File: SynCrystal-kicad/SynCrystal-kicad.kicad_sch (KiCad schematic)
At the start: 8 parts, among them Q1 BC847, U2 74HC14

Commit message: the opamp
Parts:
- added C2, C4: 100n, Capacitor_SMD:C_0805_2012Metric, symbol Device:C_Small
- added C3: 1u, Capacitor_SMD:C_0805_2012Metric, symbol Device:C_Small
- added R10: 2k2, Resistor_SMD:R_0805_2012Metric, symbol Device:R_Small
- added R11: 100, Resistor_SMD:R_0805_2012Metric, symbol Device:R_Small
- added R12: 12, Resistor_SMD:R_0805_2012Metric, symbol Device:R_Small
- added R13: 4k7, Resistor_SMD:R_0805_2012Metric, symbol Device:R_Small
- added R14, R9: 10k, Resistor_SMD:R_0805_2012Metric, symbol Device:R_Small
- added R6: 20k, Resistor_SMD:R_0805_2012Metric, symbol Device:R_Small
- added R7: 5k6, Resistor_SMD:R_0805_2012Metric, symbol Device:R_Small
- added R8: 47k, Resistor_SMD:R_0805_2012Metric, symbol Device:R_Small
- added RV1: 4k7, Potentiometer_THT:Potentiometer_Bourns_3296W_Vertical, symbol Device:R_POT_Small
- added TP1: VCTRL, TestPoint:TestPoint_THTPad_1.5x1.5mm_Drill0.7mm, symbol Connector:TestPoint
- added TP2: DAC, TestPoint:TestPoint_THTPad_1.5x1.5mm_Drill0.7mm, symbol Connector:TestPoint
- added U1: NCS20071, Package_TO_SOT_SMD:TSOT-23-5, symbol ErnoCCC-rescue:NCS20071-Amplifier_Operational
- added U3: MCP4725, Package_TO_SOT_SMD:SOT-23-6, symbol Analog_DAC:MCP4725
- added U4, U5: LMC6482, symbol Amplifier_Operational:LMC6482
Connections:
- net +5V: now also C3.2, U3.3 (VDD)
- net GNDD: now also C2.2, C3.1, C4.2, R13.1, RV1.1, RV1.2, U1.2 (V-), U3.2 (GND), U3.6 (ADR0)
- new net: R12.1, R13.2, U5.3 (+)
- new net: R6.2, R8.2, U1.4 (-)
- new net: R10.1, R14.1, U5.1
- new net: R11.2, R9.1, U5.2 (-)
- new net: R6.1, RV1.3
- new net: R7.1, U1.3 (+)
- new net: R10.2, R11.1
- new net +15V: C2.1, U1.5 (V+)
- new net 5V: C4.1, R12.2
- new net DAC: R7.2, R9.2, TP2.1, U3.1 (VOUT)
- new net SCL: U3.5 (SCL)
- new net SDA: U3.4 (SDA)
- new net VCTRL: R8.1, TP1.1, U1.1
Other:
- note added: "6-7-8"

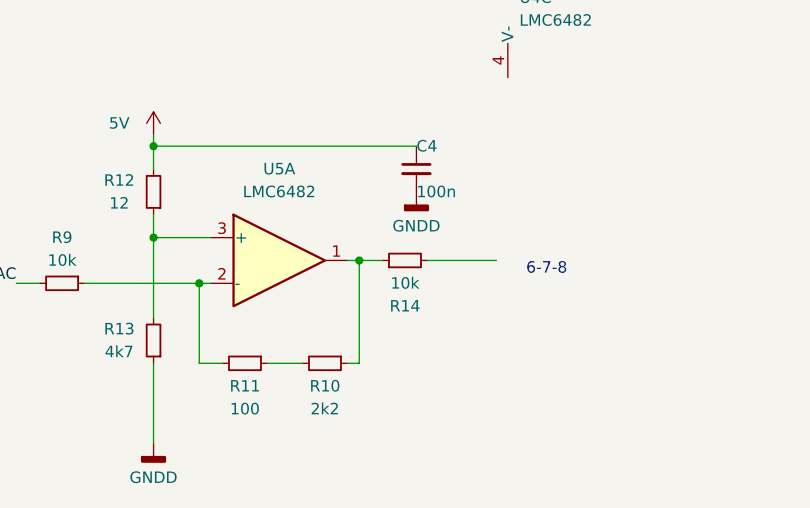
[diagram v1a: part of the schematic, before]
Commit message: Let's add some buttons
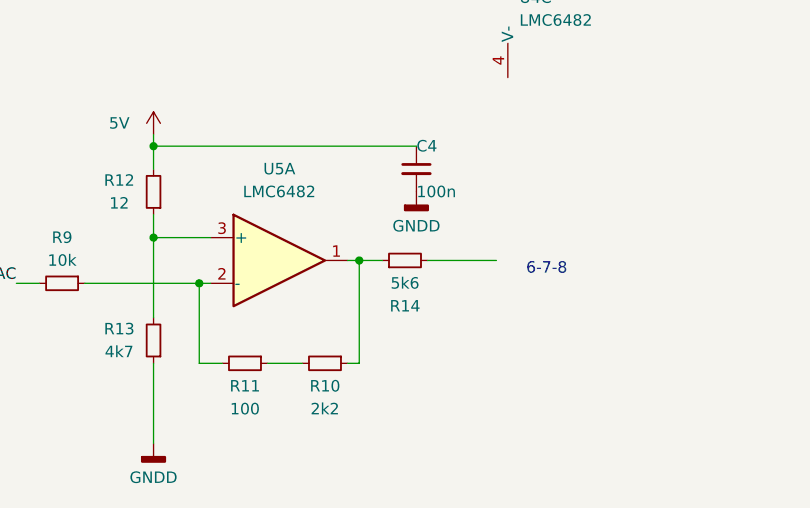
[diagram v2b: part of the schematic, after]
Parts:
- R14: value 10k -> 5k6
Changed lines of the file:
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@@
 			)
 		)
-		(property "Value" "10k"
+		(property "Value" "5k6"
 			(at 146.05 152.4 90)
 			(effects

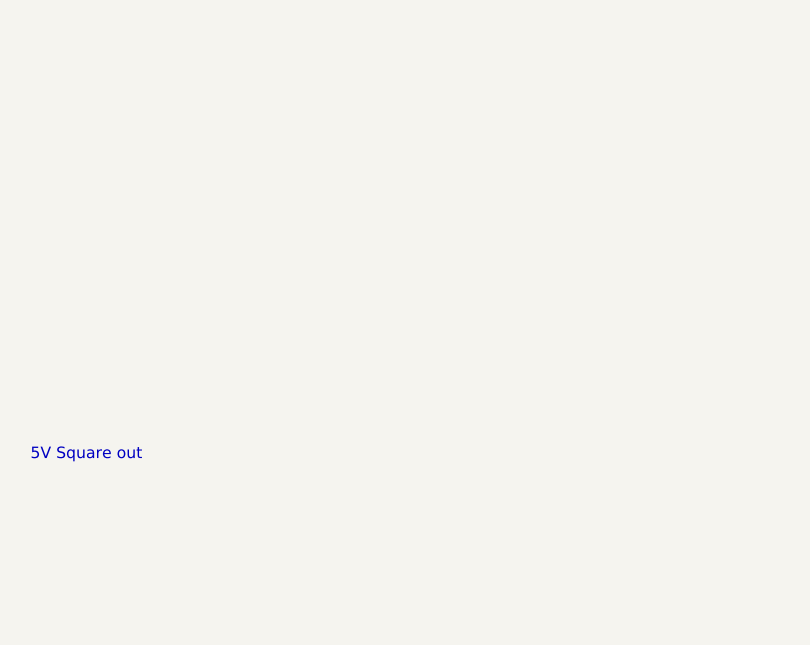
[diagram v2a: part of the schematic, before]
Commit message: adds push buttons, starts measuring DAC value lifetime
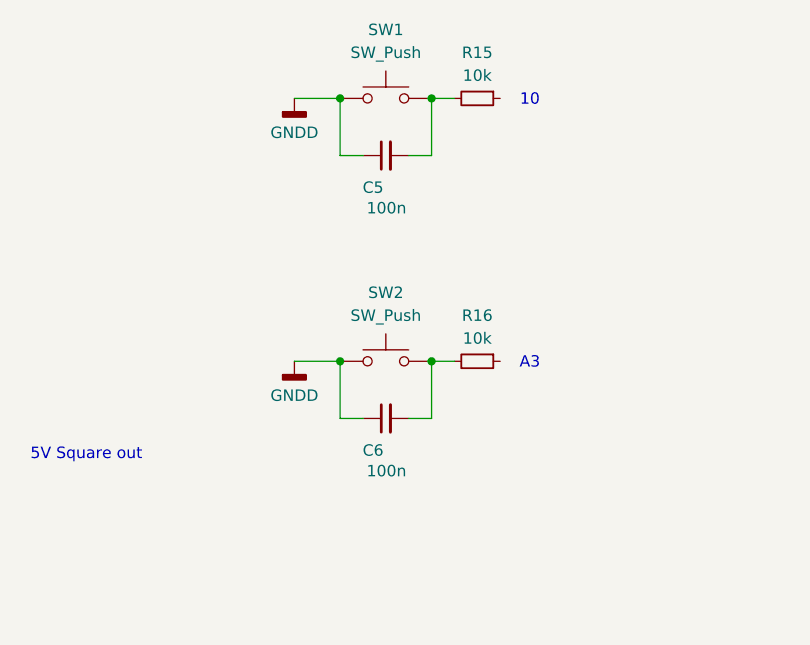
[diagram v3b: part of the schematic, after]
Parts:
- added C5, C6: 100n, Capacitor_SMD:C_0805_2012Metric, symbol Device:C_Small
- added R15, R16: 10k, Resistor_SMD:R_0805_2012Metric, symbol Device:R_Small
- added SW1, SW2: SW_Push, symbol Switch:SW_Push
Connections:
- net GNDD: now also C5.1, C6.1, SW1.1, SW2.1
- new net: C5.2, R15.2, SW1.2
- new net: C6.2, R16.2, SW2.2
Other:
- note added: "10"
- note added: "A3"

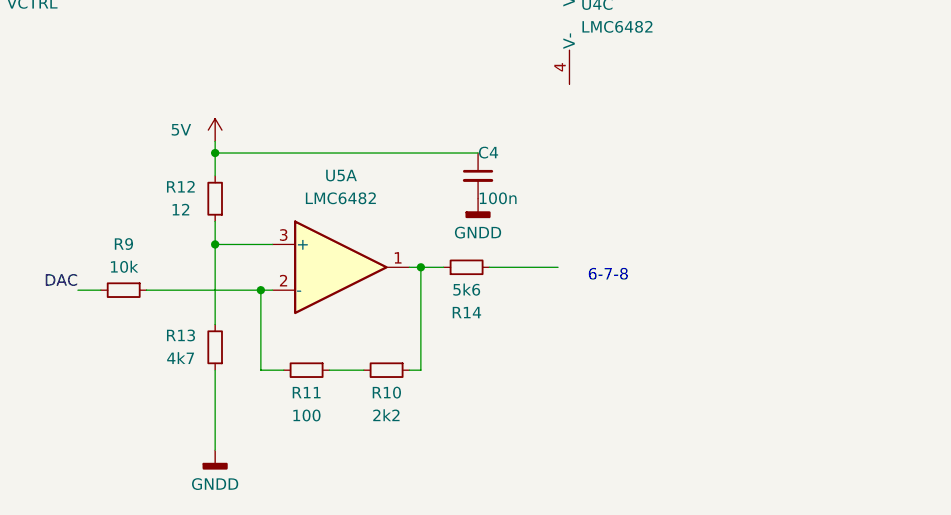
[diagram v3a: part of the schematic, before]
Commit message: adding switch to kicad
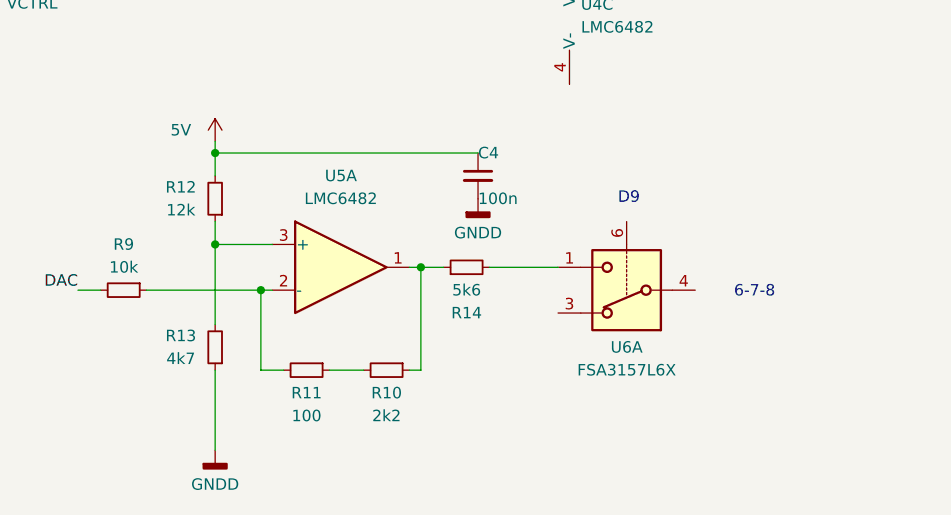
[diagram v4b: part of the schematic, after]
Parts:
- added U6: FSA3157L6X, Package_SON:Fairchild_MicroPak-6_1.0x1.45mm_P0.5mm, symbol Analog_Switch:FSA3157L6X
- R12: value 12 -> 12k
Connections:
- net at R14.2: now also U6.1
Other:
- note added: "D9"
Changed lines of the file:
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@@
 	(text "6-7-8"
 		(exclude_from_sim no)
-		(at 161.798 150.876 0)
+		(at 178.054 152.654 0)
+		(effects
+			(font
+				(size 1.27 1.27)
+			)
+		)
+	)
+	(text "D9"
+		(exclude_from_sim no)
+		(at 164.084 142.24 0)
 		(effects
 			(font
@@
 			)
 		)
-		(property "Value" "12"
+		(property "Value" "12k"
 			(at 114.3 143.51 0)
 			(effects
@@
 					(unit 1)
 				)
+			)
+		)
+	)
+	(symbol
+		(lib_id "Analog_Switch:FSA3157L6X")
+		(at 163.83 152.4 180)
+		(unit 1)
+		(exclude_from_sim no)
+		(in_bom yes)
+		(on_board yes)
+		(dnp no)
+		(fields_autoplaced yes)
+		(property "Reference" "U6"
+			(at 163.83 158.75 0)
+			(effects
+				(font
+					(size 1.27 1.27)
+				)
+			)
+		)
+		(property "Value" "FSA3157L6X"
+			(at 163.83 161.29 0)
+			(effects
+				(font
+					(size 1.27 1.27)
+				)
+			)
+		)
+		(property "Footprint" "Package_SON:Fairchild_MicroPak-6_1.0x1.45mm_P0.5mm"
+			(at 163.195 139.065 0)
+			(effects
+				(font
+					(size 1.27 1.27)
+				)
+				(justify left)
+				(hide yes)
+			)
+		)
+		(property "Datasheet" "https://www.onsemi.com/pub/Collateral/NC7SB3157-D.PDF"
+			(at 163.195 140.97 0)
+			(effects
+				(font
+					(size 1.27 1.27)
+				)
+				(justify left)
+				(hide yes)
+			)
+		)
+		(property "Description" "Single SPDT Low-Voltage Analog Switch or 2:1 Multiplexer/De-Multiplexer Bus Switch, 10Ohm Ron, MicroPak-6"
+			(at 163.83 152.4 0)
+			(effects
+				(font
+					(size 1.27 1.27)
+				)
+				(hide yes)
+			)
+		)
+		(pin "3"
+		)
+		(pin "5"
+		)
+		(pin "2"
+		)
+		(pin "4"
+		)
+		(pin "6"
+		)
+		(pin "1"
+		)
+		(instances
+			(project "SynCrystal-kicad"
+				(path "/904e3c46-2ed3-4778-9ca9-733b218304b0"
+					(reference "U6")
+					(unit 1)
+				)

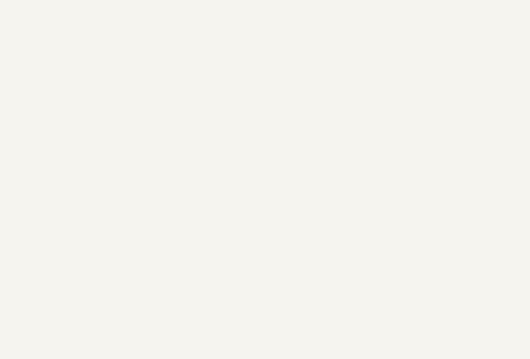
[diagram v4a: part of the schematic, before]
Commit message: First FreqMeasure-based run detection, still freewheeling though — second start is hence measuered wrong.
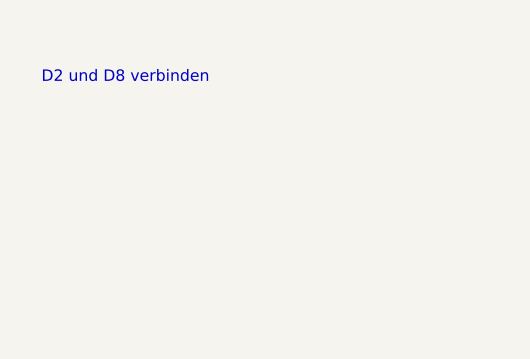
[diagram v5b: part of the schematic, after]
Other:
- note added: "D2 und D8 verbinden"
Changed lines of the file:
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@@
+		)
+	)
+	(text "D2 und D8 verbinden"
+		(exclude_from_sim no)
+		(at 48.514 33.274 0)
+		(effects
+			(font
+				(size 1.27 1.27)
+			)
 		)
 	)

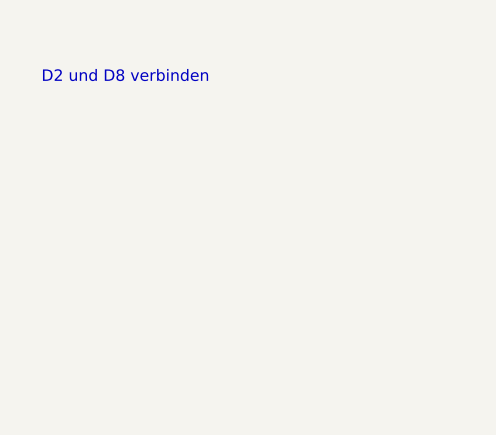
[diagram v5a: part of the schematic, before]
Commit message: add scope test pin on d7
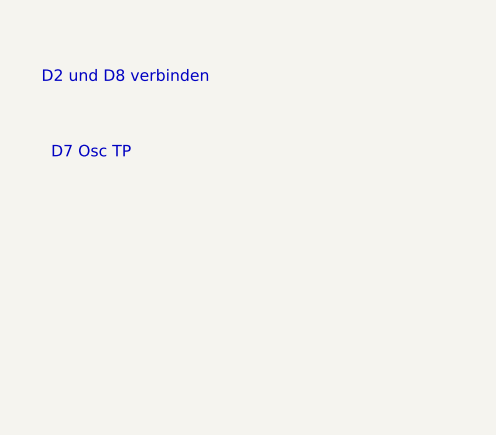
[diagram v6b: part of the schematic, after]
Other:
- note added: "D7 Osc TP"
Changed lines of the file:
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@@
+		)
+	)
+	(text "D7 Osc TP"
+		(exclude_from_sim no)
+		(at 44.704 41.656 0)
+		(effects
+			(font
+				(size 1.27 1.27)
+			)
 		)
 	)
